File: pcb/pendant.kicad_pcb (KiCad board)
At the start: 4 copper layers, 56.5 x 26.5 mm, 249 parts, among them J1 Conn_01x02, J2 USB_B_Micro, U1 ATSAMD21G18A-A, U2 LSM6DS3, U3 XC6206PxxxMR, U4 TP4057

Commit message: Revise PCB
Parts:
- added TP36: TestPoint, TestPoint:TestPoint_THTPad_D2.0mm_Drill1.0mm, F.Cu at (93.1, 84.0)
- added TP37: TestPoint, TestPoint:TestPoint_THTPad_D2.0mm_Drill1.0mm, F.Cu at (89.6, 84.0)
- added TP38: TestPoint, TestPoint:TestPoint_THTPad_D2.0mm_Drill1.0mm, F.Cu at (86.1, 84.0)
- added TP39: TestPoint, TestPoint:TestPoint_THTPad_D2.0mm_Drill1.0mm, F.Cu at (82.6, 84.0)
- added TP40: TestPoint, TestPoint:TestPoint_THTPad_D2.0mm_Drill1.0mm, F.Cu at (79.1, 84.0)
- added TP41: TestPoint, TestPoint:TestPoint_Pad_D3.0mm, F.Cu at (97.1, 89.8)
- added TP42: TestPoint, TestPoint:TestPoint_Pad_D3.0mm, F.Cu at (91.6, 89.8)
- added TP43: TestPoint, TestPoint:TestPoint_Pad_D3.0mm, F.Cu at (86.1, 89.8)
- added TP44: TestPoint, TestPoint:TestPoint_Pad_D3.0mm, F.Cu at (80.6, 89.8)
- added TP45: TestPoint, TestPoint:TestPoint_Pad_D3.0mm, F.Cu at (75.1, 89.8)
- added swd: Board, kikit:Board, F.Cu at (86.1, 81.8)
- moved TP1 0.75 mm to (93.9, 52.9)
- moved C1 0.50 mm to (91.6, 56.5)
- moved C10 0.50 mm to (95.8, 66.9)
- moved C11 0.50 mm to (95.2, 68.2)
- moved C2 0.50 mm to (98.2, 55.5)
- moved C3 0.50 mm to (110.4, 57.6)
- moved C4 0.50 mm to (112.0, 57.6)
- moved C5 0.50 mm to (104.2, 55.8)
- moved C6 0.50 mm to (104.2, 56.8)
- moved C7 0.50 mm to (95.0, 63.8)
- moved C8 0.50 mm to (100.4, 56.3)
- moved C9 0.50 mm to (105.8, 59.0)
- moved G*** 0.50 mm to (92.9, 65.9)
- moved J1 0.50 mm to (91.5, 60.5)
- moved J2 0.50 mm to (100.9, 70.7)
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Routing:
- net +3V3: track 63.4 -> 70.7 mm
- net /SWDIO: track 18.0 -> 25.1 mm
- net GND: track 9.75 -> 16.6 mm
- net /SWCLK: track 9.40 -> 16.0 mm
- net /RESET: track 7.41 -> 13.9 mm
- net /R3: track 55.1 -> 58.9 mm, vias 3 -> 2
- net /STDBY: track 23.9 -> 21.7 mm
- net /R4: track 47.5 -> 49.6 mm, vias 4 -> 2
- net /R5: track 76.2 -> 78.0 mm
- net /R1: track 49.4 -> 50.6 mm
- net /R12: track 65.5 -> 66.7 mm
- net Net-(J2-D+): track 17.2 -> 18.1 mm
- net /R13: track 61.7 -> 60.8 mm, vias 13 -> 12
- net /M15: track 10.1 -> 10.9 mm
- net /M3: track 9.39 -> 10.2 mm
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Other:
- board size 56.5 x 26.5 mm -> 56 x 44.5 mm

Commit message: Format schematic
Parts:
- turned C10 to 180 degrees
- turned C11 to 180 degrees
- turned C3 to -90 degrees
- turned C4 to -90 degrees
- turned R23 to 180 degrees
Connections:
- C10 pad 1: GND -> +3V3
- C10 pad 2: +3V3 -> GND
- C11 pad 1: GND -> VBUS
- C11 pad 2: VBUS -> GND
- C3 pad 1: VBUS -> GND
- C3 pad 2: GND -> VBUS
- C4 pad 1: +BATT -> GND
- C4 pad 2: GND -> +BATT
- R23 pad 1: /STDBY -> +3V3
- R23 pad 2: +3V3 -> /STDBY

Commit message: Check values
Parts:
- removed back, front, swd: Board, kikit:Board
- C1, C2: value 2.2 uF -> 1 uF
- R1, R10, R11, R12, R13, R14, R15, R2, R3, R4, R5, R6, R7, R8, R9: value 49.9 -> 75
- R18, R19: value 4.7k -> 10k
- R21: value 15k -> 22k
- moved TP36 3.00 mm to (93.1, 81.0)
- moved TP37 3.00 mm to (89.6, 81.0)
- moved TP38 3.00 mm to (86.1, 81.0)
- moved TP39 3.00 mm to (82.6, 81.0)
- moved TP40 3.00 mm to (79.1, 81.0)
- moved TP41 3.00 mm to (97.1, 86.8)
- moved TP42 3.00 mm to (91.6, 86.8)
- moved TP43 3.00 mm to (86.1, 86.8)
- moved TP44 3.00 mm to (80.6, 86.8)
- moved TP45 3.00 mm to (75.1, 86.8)
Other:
- board size 56 x 44.5 mm -> 56 x 41.5 mm

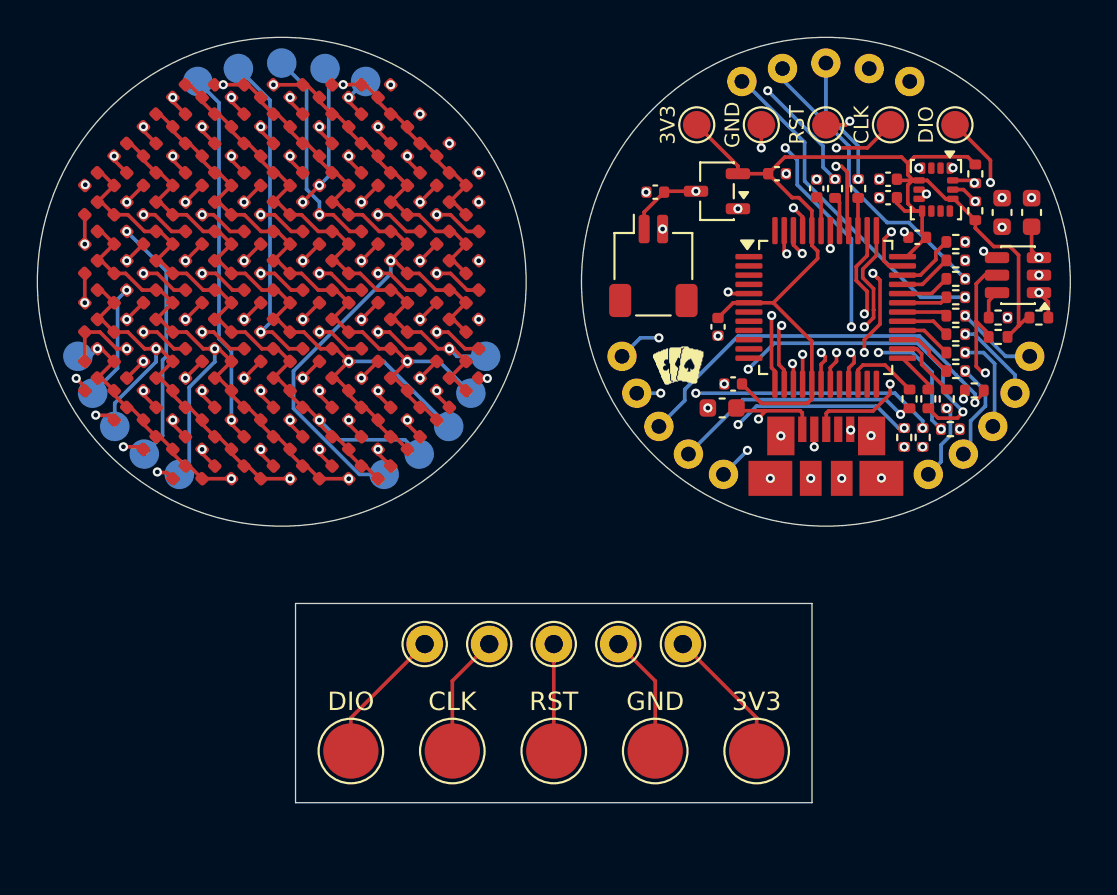
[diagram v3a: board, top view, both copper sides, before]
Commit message: Adjust SWD pad pitch
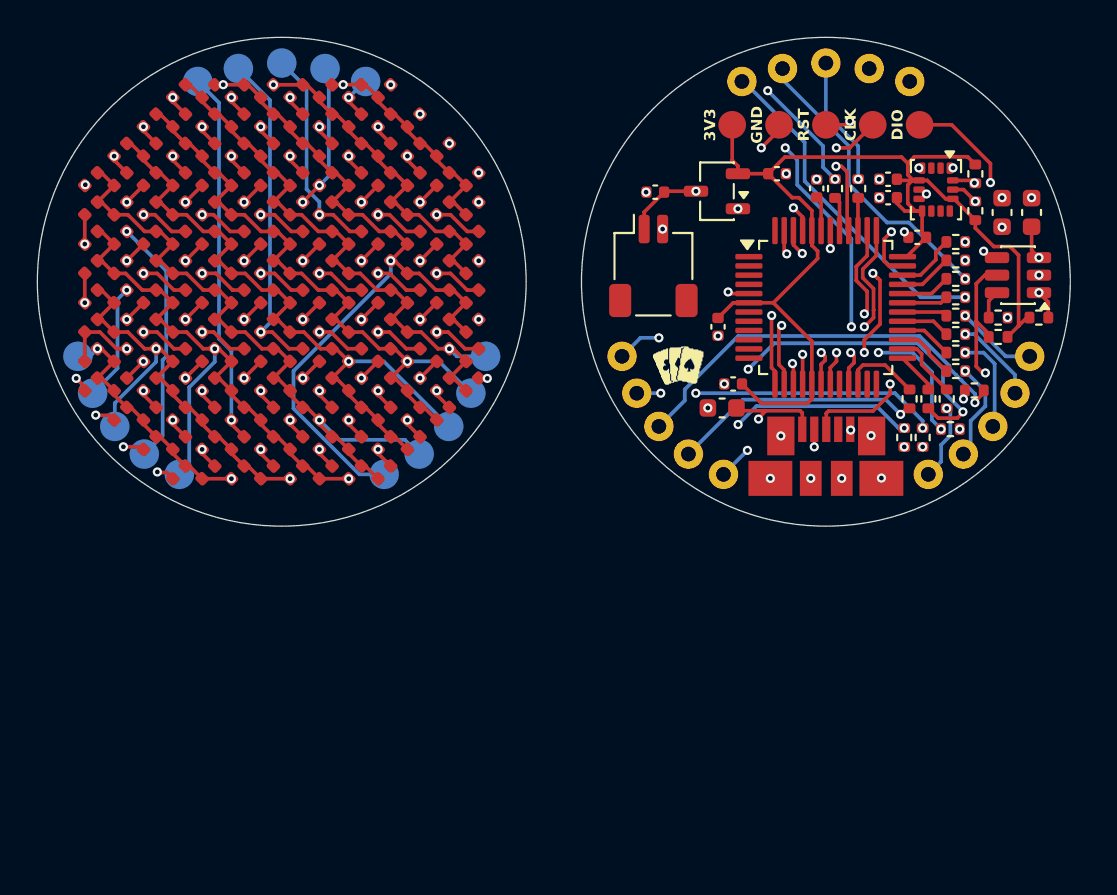
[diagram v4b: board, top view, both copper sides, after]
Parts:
- removed TP36, TP37, TP38, TP39, TP40: TestPoint, TestPoint:TestPoint_THTPad_D2.0mm_Drill1.0mm
- removed TP41, TP42, TP43, TP44, TP45: TestPoint, TestPoint:TestPoint_Pad_D3.0mm
- R21: value 22k -> 75k
- TP1, TP2, TP3, TP4, TP5: footprint TestPoint:TestPoint_Pad_D1.5mm -> Project:Pad_SMD_1.5x1.5
- moved TP1 1.92 mm to (95.8, 52.9)
- moved TP5 1.92 mm to (105.9, 52.9)
- moved TP2 0.96 mm to (98.3, 52.9)
- moved TP4 0.96 mm to (103.4, 52.9)
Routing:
- net +3V3: track 70.7 -> 62.5 mm
- net /SWCLK: track 16.0 -> 8.19 mm
- net GND: track 16.6 -> 10.4 mm
- net /RESET: track 13.9 -> 8.09 mm
- net /SWDIO: track 25.1 -> 19.5 mm
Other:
- board size 56 x 41.5 mm -> 56 x 26.5 mm
